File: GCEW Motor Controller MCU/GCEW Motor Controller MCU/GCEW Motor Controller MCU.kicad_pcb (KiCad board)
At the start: 2 copper layers, 9 parts, among them J1 POWER IN, J2 MC2, J3 MC1, J4 Programmer, U1 ATmega328PB-AU, U2 HC-05_BluetoothModule

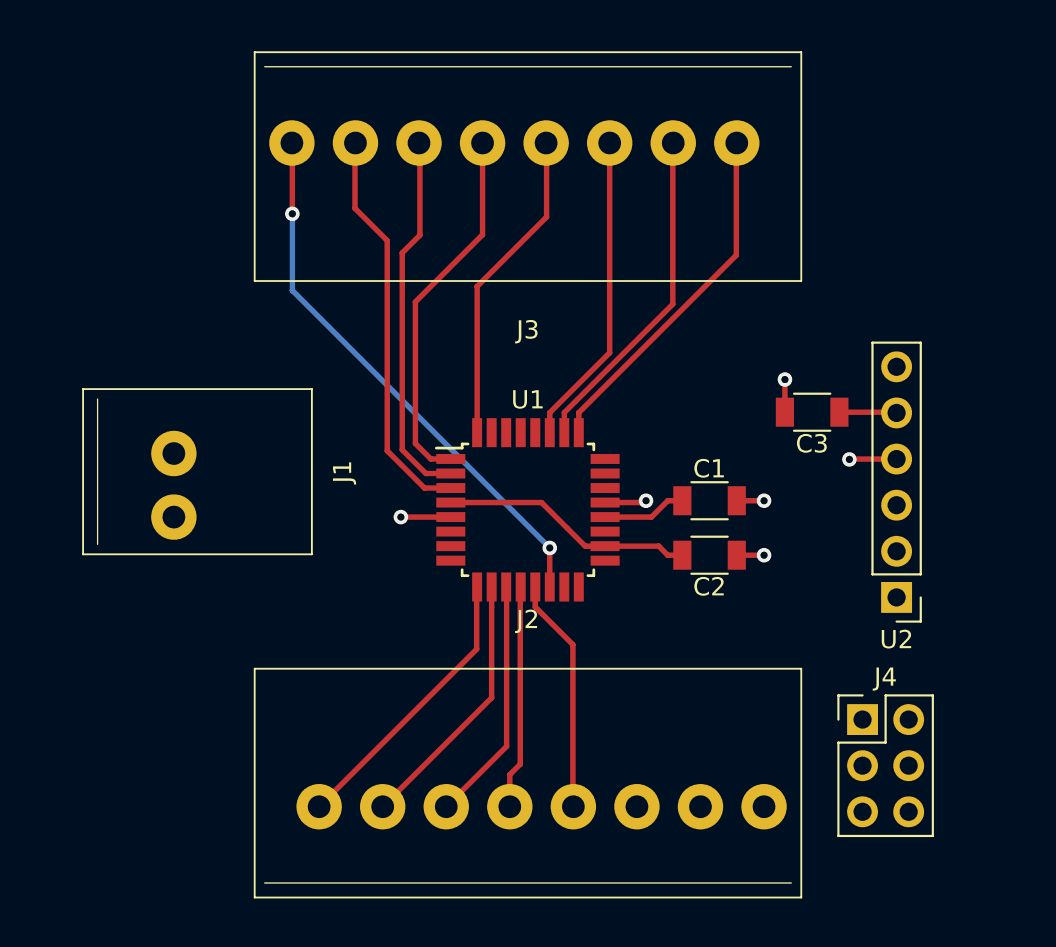
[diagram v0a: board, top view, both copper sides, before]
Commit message: GCEW Motor Controller MCU PCB Update 1
Finished PCB track layout. Need to finish adding text to bottom silkscreen layer.
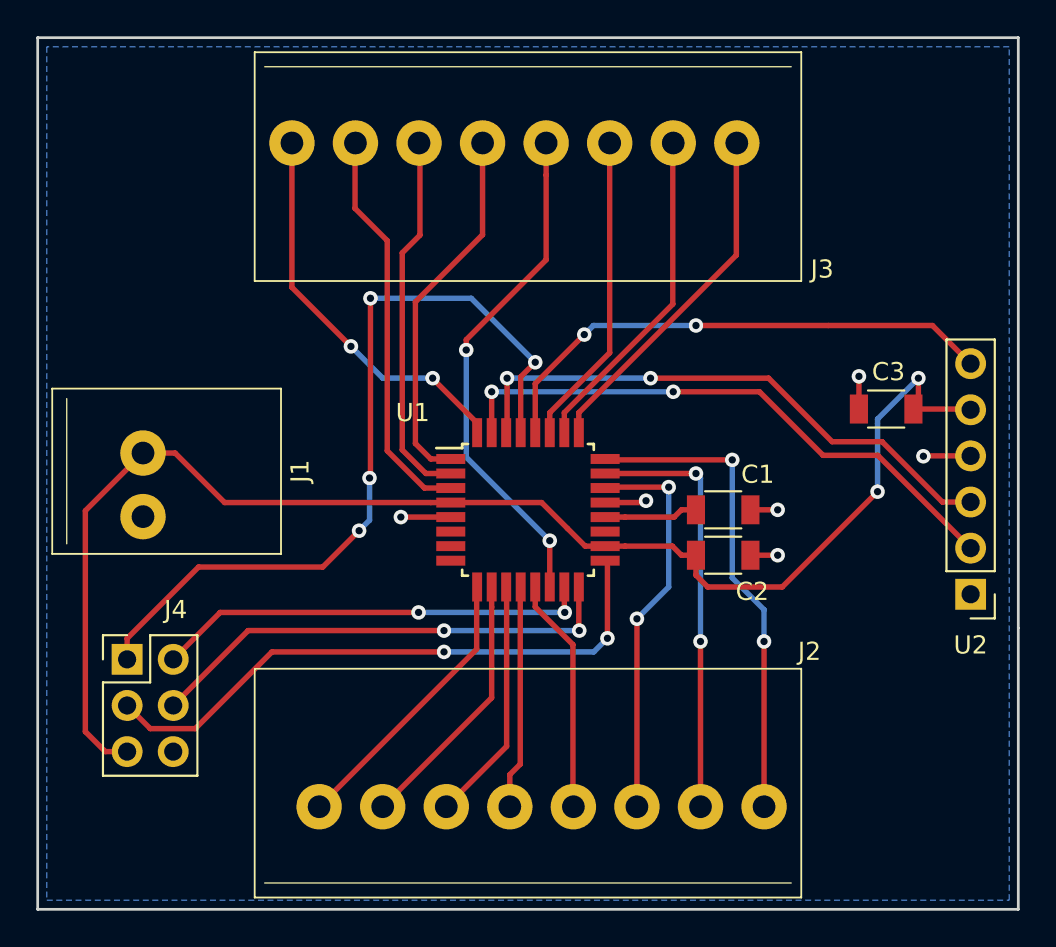
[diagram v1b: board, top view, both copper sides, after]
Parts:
- moved J4 40.6 mm to (143.4, 101.2)
- moved C3 4.08 mm to (185.2, 87.5)
- moved U2 4.08 mm to (189.9, 97.7)
- moved J1 1.70 mm to (145.6, 90.9)
- moved C1 0.90 mm to (176.2, 93.0)
- moved C2 0.75 mm to (176.2, 95.5)
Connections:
- J4 pad 1: MOSI -> ~RESET
- J4 pad 2: MISO -> MOSI
- J4 pad 4: ~RESET -> MISO
- U1 pad 14: INHA2 -> ENABLE2
- U1 pad 32: ENABLE2 -> INHA2
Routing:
- net +5V: track 17.3 -> 78.1 mm, vias 0 -> 2
- net ~RESET: track 0.00 -> 44.2 mm, vias 0 -> 4
- net SCK: track 0.00 -> 33.4 mm, vias 0 -> 2
- net HC-05_RX: track 0.00 -> 32.2 mm, vias 0 -> 2
- net HC-05_TX: track 0.00 -> 31.4 mm, vias 0 -> 2
- net PC5: track 0.00 -> 28.9 mm, vias 0 -> 2
- net SOA1: track 0.00 -> 26.8 mm, vias 0 -> 2
- net MISO: track 0.00 -> 26.5 mm, vias 0 -> 2
- net MOSI: track 0.00 -> 24.0 mm, vias 0 -> 2
- net SOB1: track 0.00 -> 23.5 mm, vias 0 -> 2
- net SOC1: track 0.00 -> 21.8 mm, vias 0 -> 2
- net ENABLE2: track 17.4 -> 28.2 mm, vias 0 -> 2
- net INHA2: track 30.3 -> 21.8 mm
- added copper zone on B.Cu, net GND
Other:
- board outline added: 54 x 48 mm
- board text added: "5V"
- board text added: "CAL1"
- board text added: "EN1"
- board text added: "GND"
- board text added: "INHA1"
- board text added: "INHC1"
- board text added: "INLC1"
- board text added: "MISO"
- board text added: "MOSI"
- board text added: "SCK"
- board text added: "SOA1"
- board text added: "SOB1"
- board text added: "SOC1"
- board text added: "~Reset"
